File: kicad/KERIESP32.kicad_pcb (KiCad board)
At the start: 2 copper layers, 76.2 x 33 mm, 11 parts, among them P1 CONN_01X30, SW1 RESET, SW2 IO0, U1 NJM2884, U2 ESP-WROOM-32

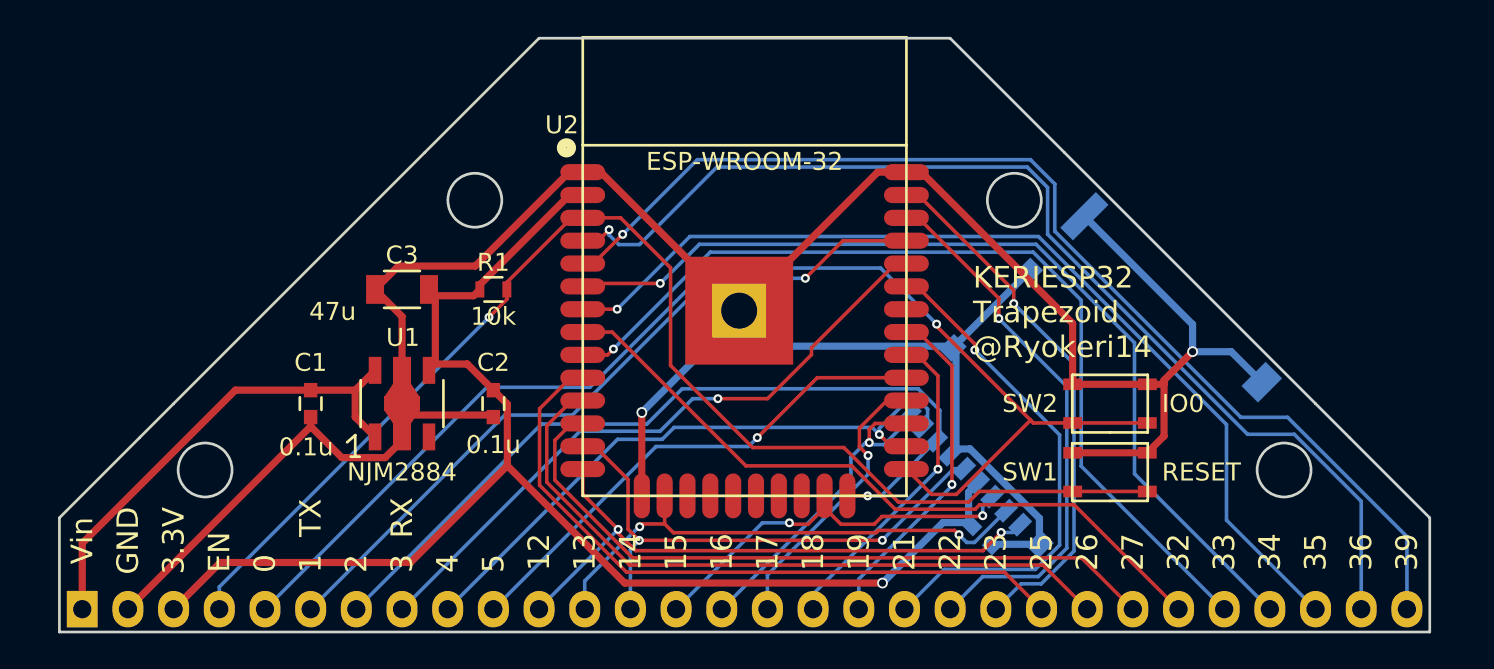
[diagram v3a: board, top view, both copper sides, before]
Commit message: ブレッドボード用の基板を設計SIP
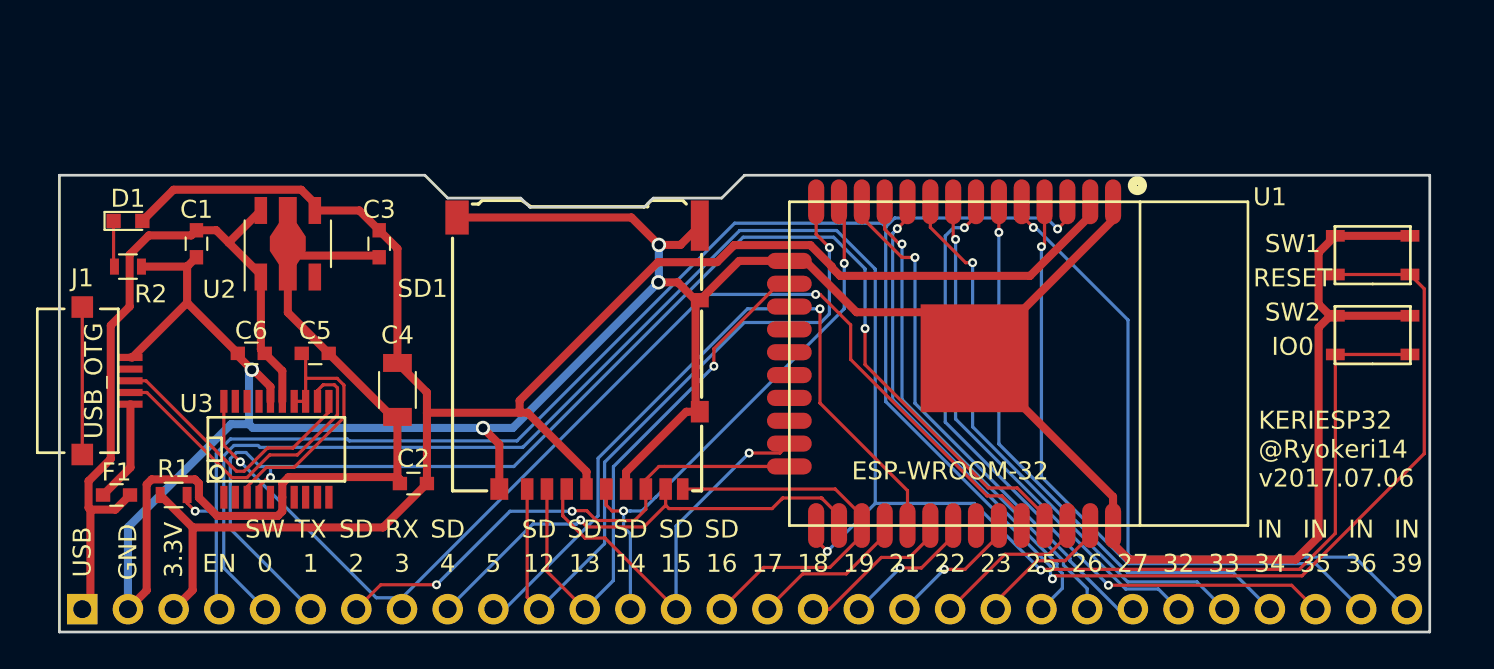
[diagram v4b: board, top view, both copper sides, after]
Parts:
- removed the U2 at (157.5, 100.3)
- added C5: 0.1u, Capacitors_SMD:C_0603, F.Cu at (133.6, 105.2)
- added C6: 0.1u, Capacitors_SMD:C_0603, F.Cu at (130.0, 105.2)
- added D1: Power, LEDs:LED_0603, F.Cu at (123.2, 97.8)
- added F1: FEMTOSMDC035F-02, Capacitors_SMD:C_0603, F.Cu at (122.6, 113.0)
- added J1: USB_OTG, KERIESP32:ZX62R-B-5P, F.Cu at (120.7, 106.7)
- added R2: 1k, Resistors_SMD:R_0603, F.Cu at (123.2, 100.3)
- added U1: ESP-WROOM-32, KERIESP32:ESP-WROOM-32, F.Cu at (172.7, 105.7)
- added U3: FT231XS, SMD_Packages:SSOP-20, F.Cu at (131.4, 110.5)
- C2: renamed from C4; moved to F.Cu
- P1: value CONN_01X30 -> CONN; footprint Pin_Headers:Pin_Header_Straight_1x30 -> Pin_Headers:Pin_Header_Straight_1x30_Pitch2.54mm
- SD1: footprint kerikun11:HIROSE-MICROSD-DM3AT-SF -> KERIESP32:HIROSE-MICROSD-DM3AT-SF; moved to F.Cu
- SW1, SW2: footprint kerikun11:SW_PUSH -> KERIESP32:SW_PUSH
- moved SD1 34.6 mm to (148.6, 95.2), turned to 180 degrees
- moved C2 31.8 mm to (139.1, 112.4), turned to 180 degrees
- moved R1 21.1 mm to (125.7, 113.0)
- moved SW1 18.9 mm to (192.4, 99.7)
- moved SW2 15.1 mm to (192.4, 104.1)
- moved C1 10.9 mm to (127.0, 99.1)
- moved C3 10.9 mm to (137.2, 99.1)
- moved U2 10.9 mm to (132.1, 99.1), turned to 90 degrees
- moved C4 5.59 mm to (138.2, 107.2), turned to 270 degrees
- renumbered C2 to C3, C3 to C4, U1 to U2
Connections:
- P1 pad 6: Net-(P1-Pad6) -> TXD
- P1 pad 8: Net-(P1-Pad8) -> RXD
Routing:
- net TXD: track 0.00 -> 73.4 mm, vias 0 -> 2
- net RXD: track 0.00 -> 64.7 mm, vias 0 -> 2
- net GND: track 168.5 -> 227.4 mm, vias 2 -> 4
- net ENABLE: track 71.9 -> 126.9 mm, vias 1 -> 3
- net IO0: track 69.8 -> 112.4 mm, vias 1 -> 2
- net Net-(P1-Pad6): track 41.6 -> 0.00 mm, vias 1 -> 0
- net Net-(P1-Pad8): track 36.2 -> 0.00 mm, vias 1 -> 0
- net Net-(P1-Pad29): track 61.1 -> 36.2 mm
- net +3V3: track 78.2 -> 102.4 mm, vias 1 -> 0
- net Net-(P1-Pad30): track 62.5 -> 38.9 mm
- net Net-(P1-Pad21): track 29.7 -> 7.74 mm, vias 1 -> 0
- net Net-(P1-Pad20): track 30.3 -> 8.78 mm, vias 1 -> 0
- net Net-(P1-Pad19): track 28.4 -> 7.50 mm
- net Net-(P1-Pad26): track 51.7 -> 31.9 mm
- net Net-(P1-Pad27): track 51.9 -> 32.3 mm
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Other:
- board size 76.2 x 33 mm -> 76.2 x 25.4 mm
- net class Default: clearance 0.2 -> 0.18; trace_width 0.2 -> 0.18
- net class Power: clearance 0.2 -> 0.18; trace_width 0.4 -> 0.45; via_dia 0.6 -> 0.8; via_drill 0.4 -> 0.5
- rule trace_clearance: 0.2 -> 0.18
- rule trace_min: 0.2 -> 0.18
- board text added: "IN"
- board text added: "KERIESP32 @Ryokeri14 v2017.07.06"
- board text added: "SD"
- board text added: "SW"
- board text added: "USB"
- board text removed: "KERIESP32 Trapezoid @Ryokeri14"
- board text removed: "Vin"

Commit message: 小型化，自動配線成功
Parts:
- F1: value FEMTOSMDC035F-02 -> FEMTOSMDC035F
- J1: value USB_OTG -> ZX62R-B-5P
- P1: footprint Pin_Headers:Pin_Header_Straight_1x30_Pitch2.54mm -> KERIESP32:Pin_Header_Straight_1x30_Pitch2.54mm
- SD1: value Micro_SD -> DM3AT-SF-PEJM5
- moved C2 19.1 mm to (158.1, 113.0), turned to 90 degrees
- moved R1 14.0 mm to (139.7, 113.0)
- moved C1 6.38 mm to (127.6, 105.4), turned to 180 degrees
- moved D1 5.24 mm to (128.3, 99.1)
- moved R2 4.62 mm to (127.6, 101.6)
- moved SW1 4.45 mm to (192.4, 104.1)
- moved F1 4.44 mm to (127.0, 113.0)
- moved SW2 3.81 mm to (192.4, 108.0)
- moved J1 2.29 mm to (119.4, 108.6)
- moved C6 1.83 mm to (131.6, 106.2)
- moved C5 1.83 mm to (135.1, 106.2)
- moved U3 1.80 mm to (132.7, 111.8)
- moved SD1 1.80 mm to (149.9, 96.5)
- moved U2 1.80 mm to (133.3, 100.3)
- moved C4 1.45 mm to (139.1, 106.0)
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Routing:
- net GND: track 227.4 -> 0.00 mm, vias 4 -> 0
- net ENABLE: track 126.9 -> 0.00 mm, vias 3 -> 0
- net IO0: track 112.4 -> 0.00 mm, vias 2 -> 0
- net +3V3: track 102.4 -> 0.00 mm
- net TXD: track 73.4 -> 0.00 mm, vias 2 -> 0
- net RXD: track 64.7 -> 0.00 mm, vias 2 -> 0
- net +5V: track 42.4 -> 0.00 mm
- net Net-(P1-Pad10): track 41.0 -> 0.00 mm, vias 1 -> 0
- net SD_SD2: track 39.1 -> 0.00 mm, vias 1 -> 0
- net Net-(P1-Pad30): track 38.9 -> 0.00 mm, vias 1 -> 0
- net Net-(P1-Pad28): track 38.2 -> 0.00 mm, vias 2 -> 0
- net Net-(P1-Pad29): track 36.2 -> 0.00 mm, vias 1 -> 0
- net Net-(P1-Pad27): track 32.3 -> 0.00 mm, vias 1 -> 0
- net Net-(P1-Pad26): track 31.9 -> 0.00 mm, vias 1 -> 0
- net SD_CLK: track 31.7 -> 0.00 mm, vias 2 -> 0
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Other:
- board size 76.2 x 25.4 mm -> 76.2 x 24.1 mm
- net class Default: clearance 0.18 -> 0.16; via_dia 0.5 -> 0.6
- net class Power: clearance 0.18 -> 0.16
- rule trace_clearance: 0.18 -> 0.16
- rule trace_min: 0.18 -> 0.16
- rule via_min_size: 0.4 -> 0.6
- board text added: "KERIESP32 @Ryokeri14 v2017.07.14"
- board text removed: "KERIESP32 @Ryokeri14 v2017.07.06"

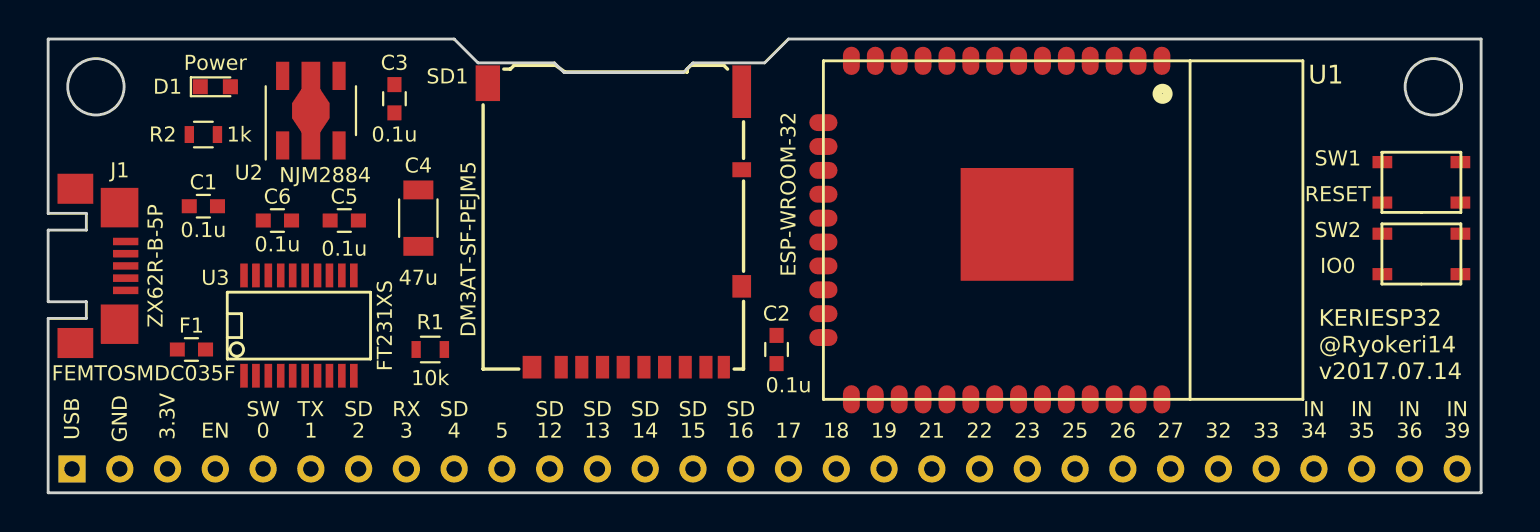
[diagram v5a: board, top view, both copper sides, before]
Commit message: マイクロSDのクリアランスの修正
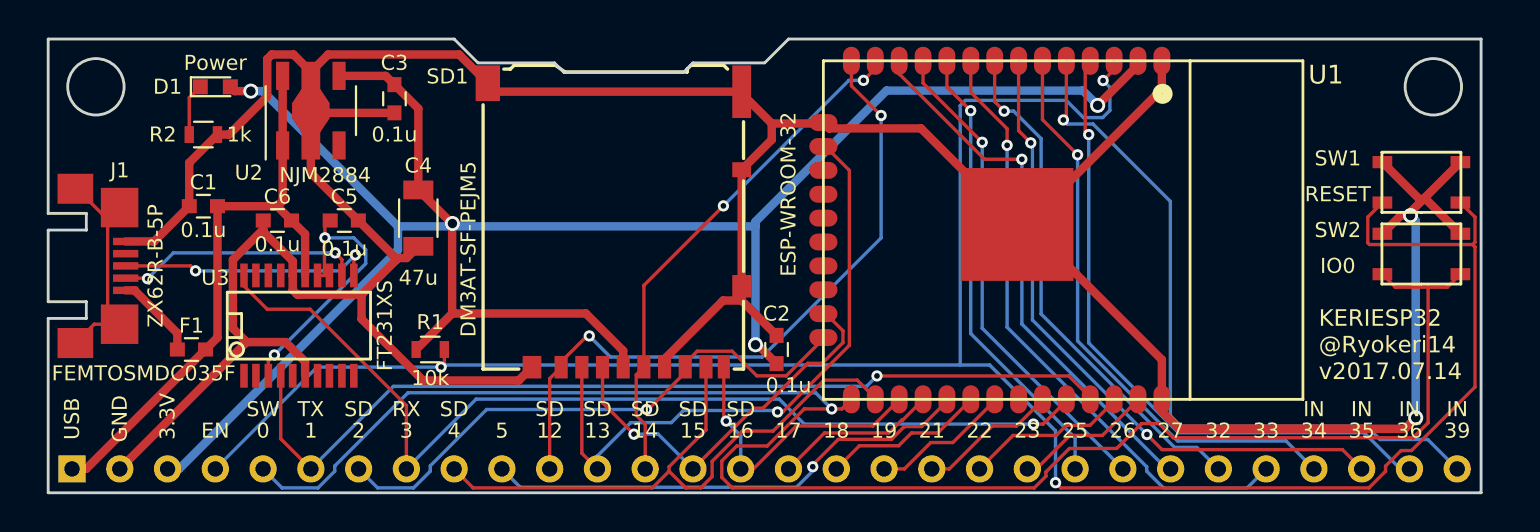
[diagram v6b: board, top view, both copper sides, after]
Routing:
- net GND: track 0.00 -> 200.0 mm, vias 0 -> 2
- net ENABLE: track 0.00 -> 120.7 mm, vias 0 -> 3
- net +3V3: track 0.00 -> 112.3 mm, vias 0 -> 4
- net IO0: track 0.00 -> 94.3 mm, vias 0 -> 1
- net RXD: track 0.00 -> 53.0 mm, vias 0 -> 1
- net TXD: track 0.00 -> 49.7 mm, vias 0 -> 1
- net Net-(P1-Pad30): track 0.00 -> 38.5 mm, vias 0 -> 1
- net SD_SD2: track 0.00 -> 36.7 mm, vias 0 -> 2
- net Net-(P1-Pad29): track 0.00 -> 35.0 mm, vias 0 -> 1
- net Net-(P1-Pad28): track 0.00 -> 34.9 mm, vias 0 -> 2
- net SD_SD3: track 0.00 -> 33.6 mm, vias 0 -> 1
- net SD_SD1: track 0.00 -> 33.2 mm
- net Net-(P1-Pad26): track 0.00 -> 32.8 mm, vias 0 -> 1
- net +5V: track 0.00 -> 32.1 mm
- net Net-(P1-Pad27): track 0.00 -> 31.1 mm, vias 0 -> 1
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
